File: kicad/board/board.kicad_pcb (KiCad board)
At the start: 4 copper layers, 58.7 x 74.9 mm, 59 parts, among them J1 i2c_connector, J2 uart_connector, J3 spi_connector, J4 debug header, J5 powerheader, J6 USB_B_Micro, J7 gpioheader A, J8 gpioheader B, SW1 reset button, SW2 pw_sw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

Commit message: adding testpoint to measure bat charge current This will make it easier to identify bat charging problems.
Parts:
- added TP4: batcurrent, TestPoint:TestPoint_Pad_D1.0mm, F.Cu at (28.7, 59.2)
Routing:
- net Net-(R1-Pad2): track 2.31 -> 14.0 mm, vias 0 -> 2

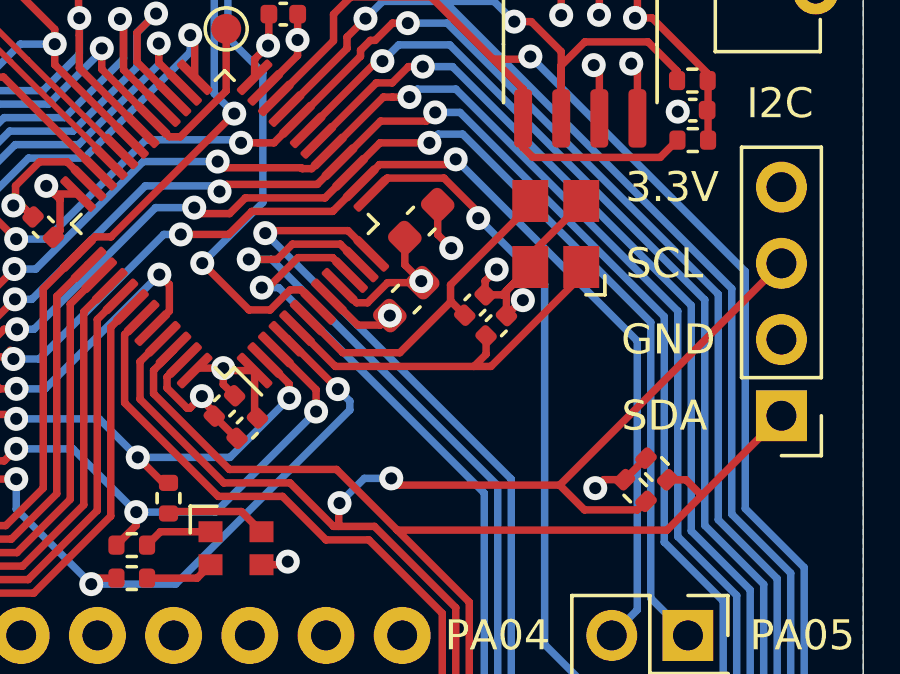
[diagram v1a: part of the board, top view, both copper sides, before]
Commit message: changing crystal for a 8MHz one instead of 16MHz
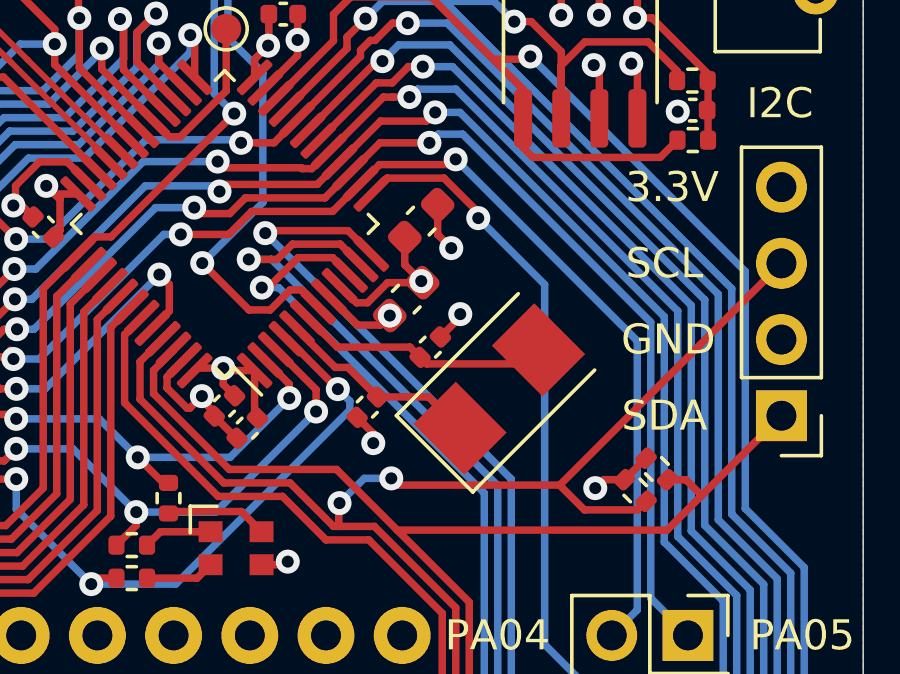
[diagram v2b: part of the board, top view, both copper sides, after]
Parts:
- C1, C2: value 8pF -> 30pF
- Y1: value X322516MLB4SI -> X50328MSB2GI; footprint components:YSX321SL -> Crystal:Crystal_SMD_5032-2Pin_5.0x3.2mm
- moved Y1 5.50 mm to (66.1, 84.5), turned to 45 degrees
- moved C1 5.08 mm to (61.7, 85.1), turned to 225 degrees
- moved C2 2.05 mm to (63.8, 83.1)
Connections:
- Y1 pad 2: GND -> Net-(C2-Pad1)
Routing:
- net GND: track 61.7 -> 55.4 mm
- net Net-(C1-Pad1): track 12.7 -> 6.84 mm
- net Net-(C2-Pad1): track 11.1 -> 8.53 mm

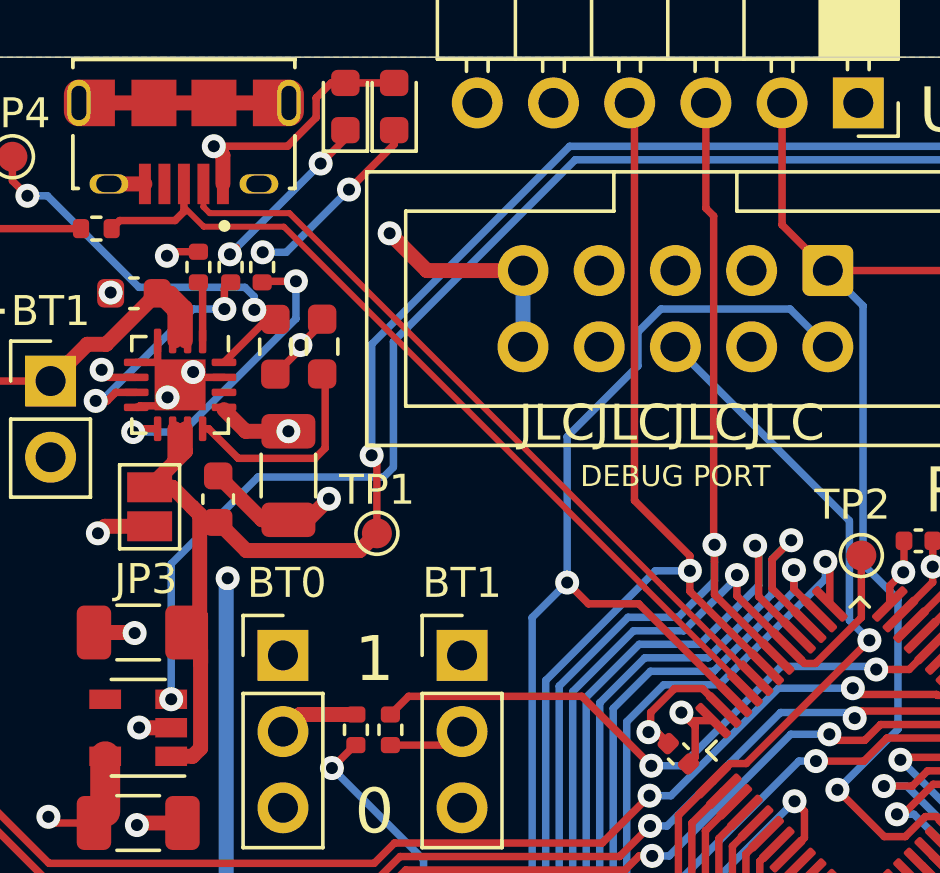
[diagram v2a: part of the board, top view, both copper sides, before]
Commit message: rewired the usb bus so the impedence is matched for JLC7628 fixing #20
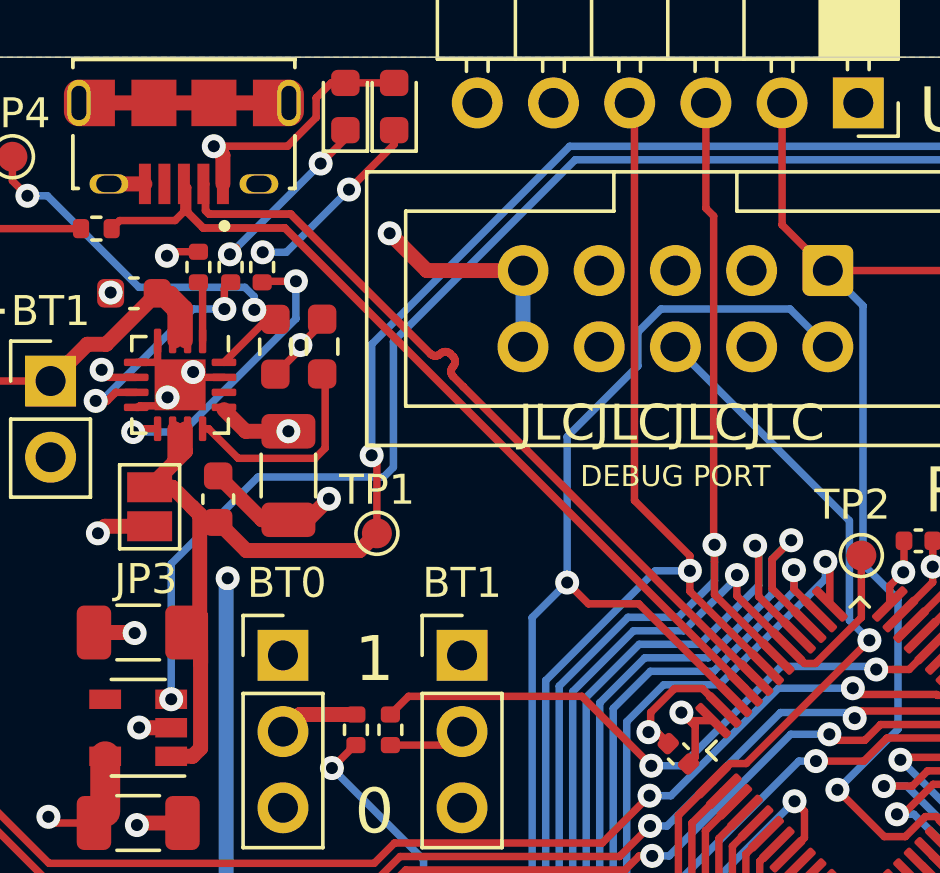
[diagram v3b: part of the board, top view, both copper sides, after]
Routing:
- net /usb_d-: track 25.7 -> 26.3 mm

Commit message: adding termite logo to back of pcb fixing #10
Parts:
- added G***: LOGO, components:logo, F.Cu at (66.1, 81.7)
